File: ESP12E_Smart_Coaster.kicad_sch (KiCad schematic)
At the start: 13 parts

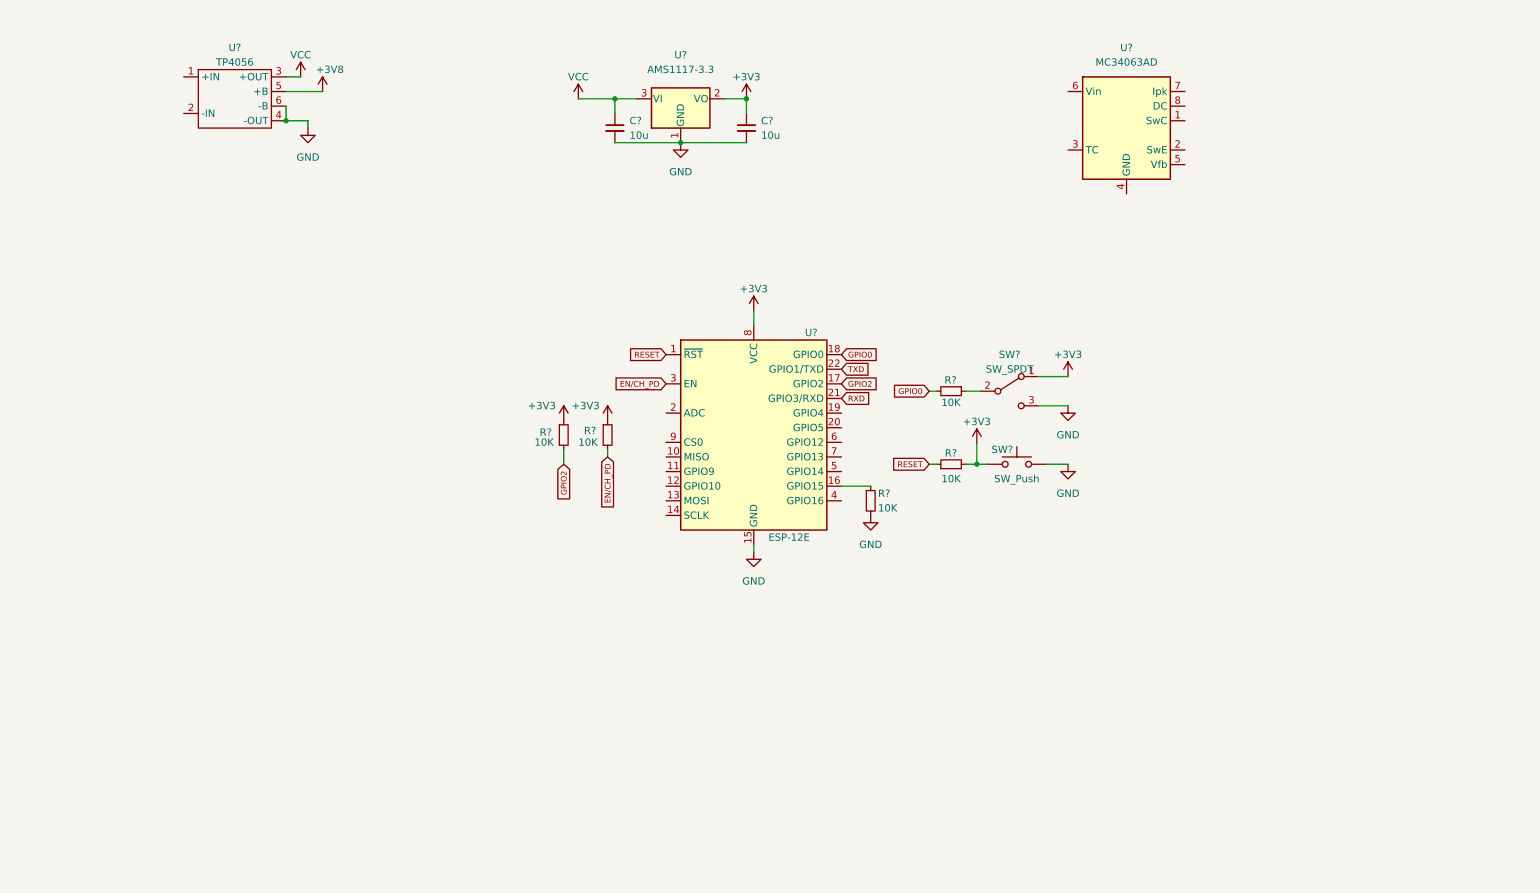
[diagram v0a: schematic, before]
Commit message: Adds WS2812B Leds & Logic Level Shifter in schematic
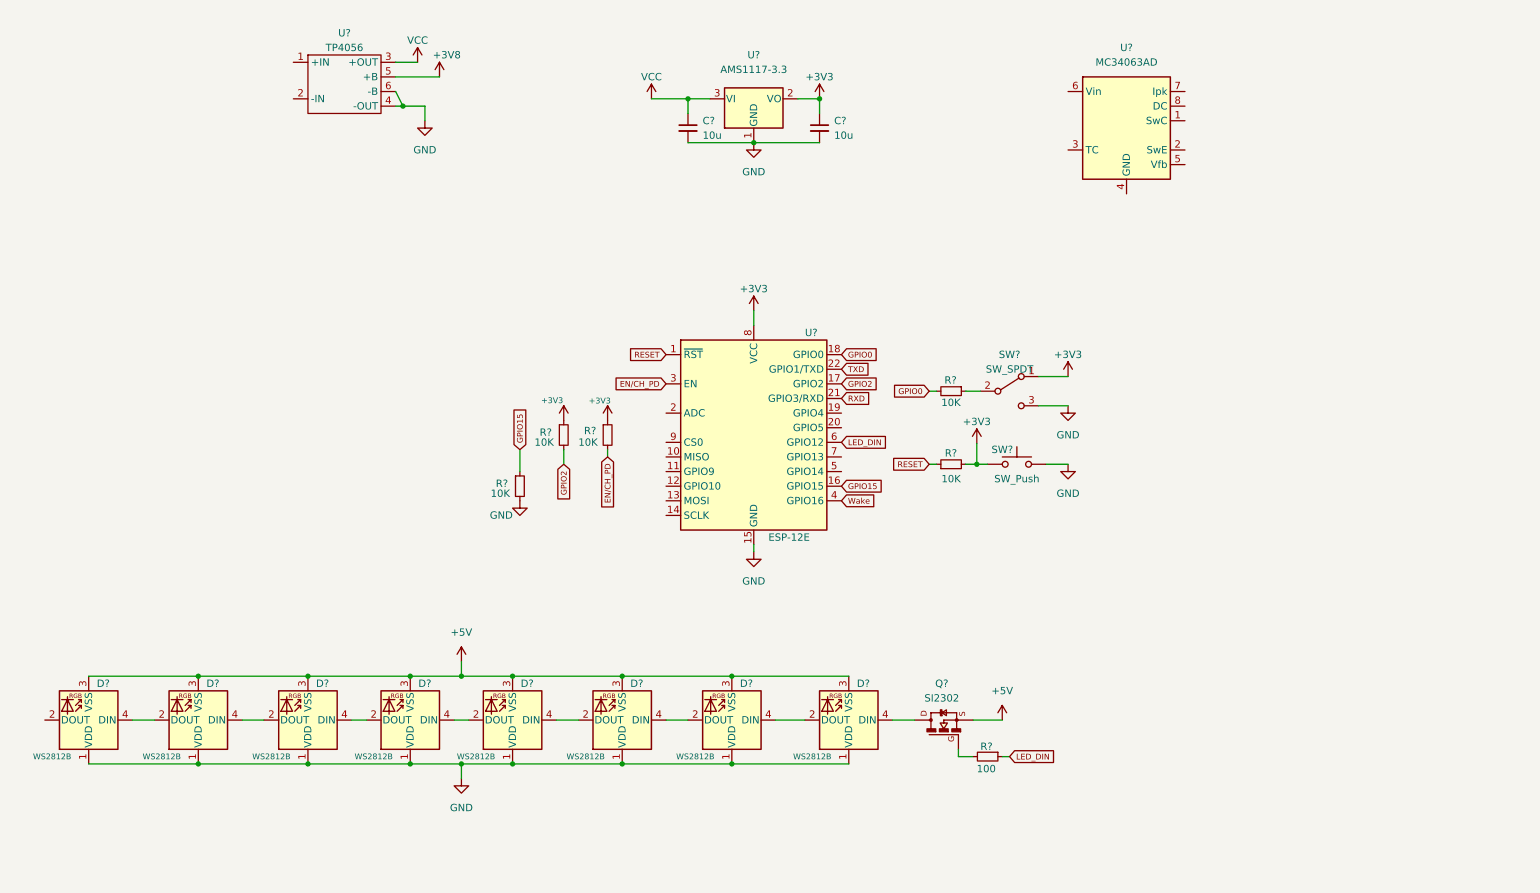
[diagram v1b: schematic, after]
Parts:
- removed R?: 10K, symbol Device:R_Small
- added D? (x8): WS2812B, LED_SMD:LED_WS2812B_PLCC4_5.0x5.0mm_P3.2mm, symbol LED:WS2812B
- added Q?: SI2302, SOT23, symbol SI2302:SI2302
- added R?: 10K, symbol Device:R_Small
- added R?: 100, symbol Device:R_Small
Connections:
- net GND: now also D?.1 (VDD), D?.1 (VDD), D?.1 (VDD), D?.1 (VDD), D?.1 (VDD), D?.1 (VDD), D?.1 (VDD), D?.1 (VDD), R?.2
- net GPIO15: now reaches U?.16 (GPIO15)
- net GPIO15: now also R?.1
- net Wake: now reaches U?.4 (GPIO16)
- net LED_DIN: now reaches U?.6 (GPIO12)
- net LED_DIN: now also R?.1
- new net: D?.2 (DOUT), D?.4 (DIN) (x7)
- new net: D?.4 (DIN), Q?.3
- new net: Q?.1, R?.2
- new net +5V: D?.3 (VSS), D?.3 (VSS), D?.3 (VSS), D?.3 (VSS), D?.3 (VSS), D?.3 (VSS), D?.3 (VSS), D?.3 (VSS), Q?.2
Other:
- moved on the sheet: C?, U?

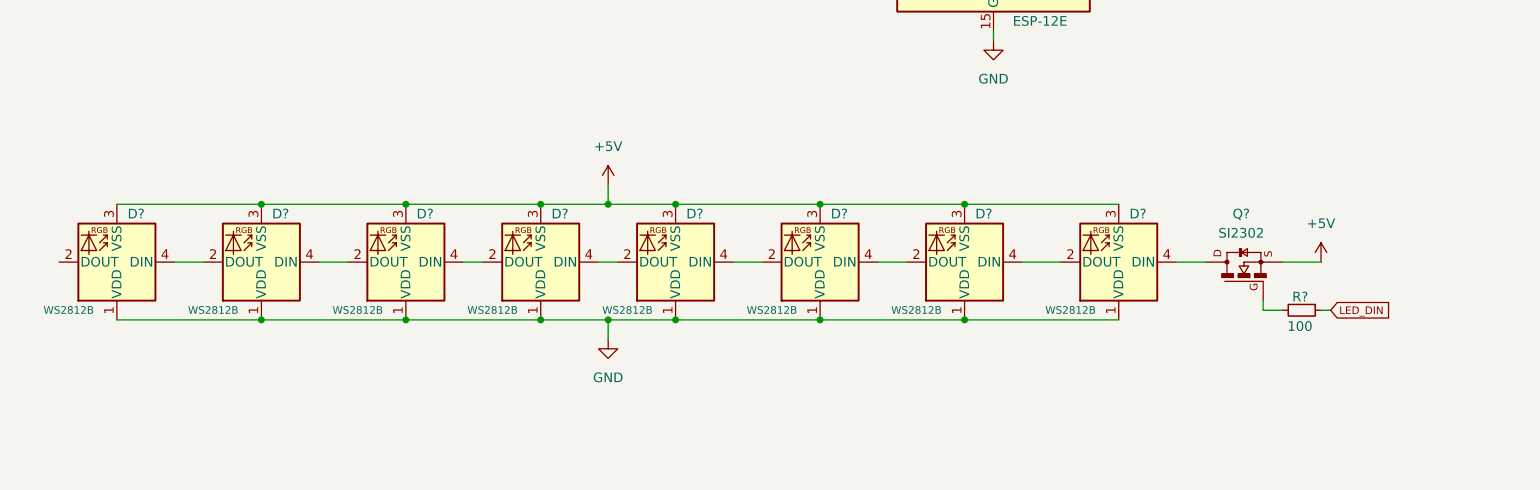
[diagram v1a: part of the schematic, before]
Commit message: Adds 0.1uF cap to WS2812B LEDs
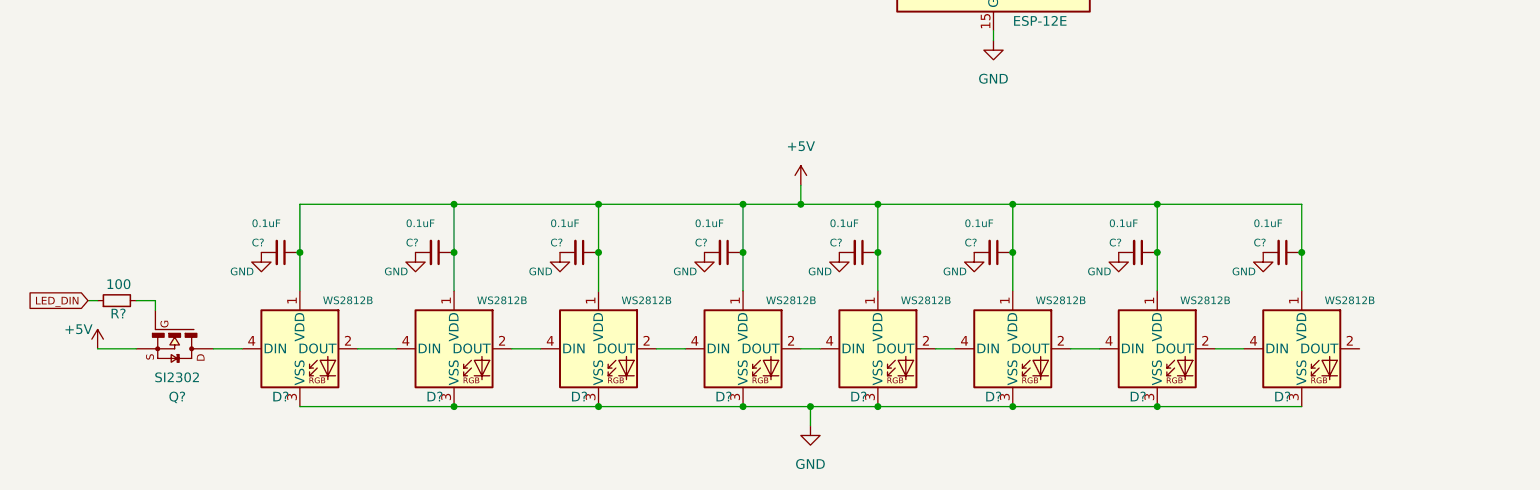
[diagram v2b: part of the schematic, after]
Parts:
- added C? (x8): 0.1uF, symbol Device:C_Small
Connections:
- net +5V: now also D?.1 (VDD), D?.1 (VDD), D?.1 (VDD), D?.1 (VDD), D?.1 (VDD), D?.1 (VDD), D?.1 (VDD), D?.1 (VDD), C?.1, C?.1, C?.1, C?.1, C?.1, C?.1, C?.1, C?.1; no longer D?.3 (VSS), D?.3 (VSS), D?.3 (VSS), D?.3 (VSS), D?.3 (VSS), D?.3 (VSS), D?.3 (VSS), D?.3 (VSS)
- net GND: now also D?.3 (VSS), D?.3 (VSS), D?.3 (VSS), D?.3 (VSS), D?.3 (VSS), D?.3 (VSS), D?.3 (VSS), D?.3 (VSS), C?.2, C?.2, C?.2, C?.2, C?.2, C?.2, C?.2, C?.2; no longer D?.1 (VDD), D?.1 (VDD), D?.1 (VDD), D?.1 (VDD), D?.1 (VDD), D?.1 (VDD), D?.1 (VDD), D?.1 (VDD)
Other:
- moved on the sheet: D?, Q?, R?

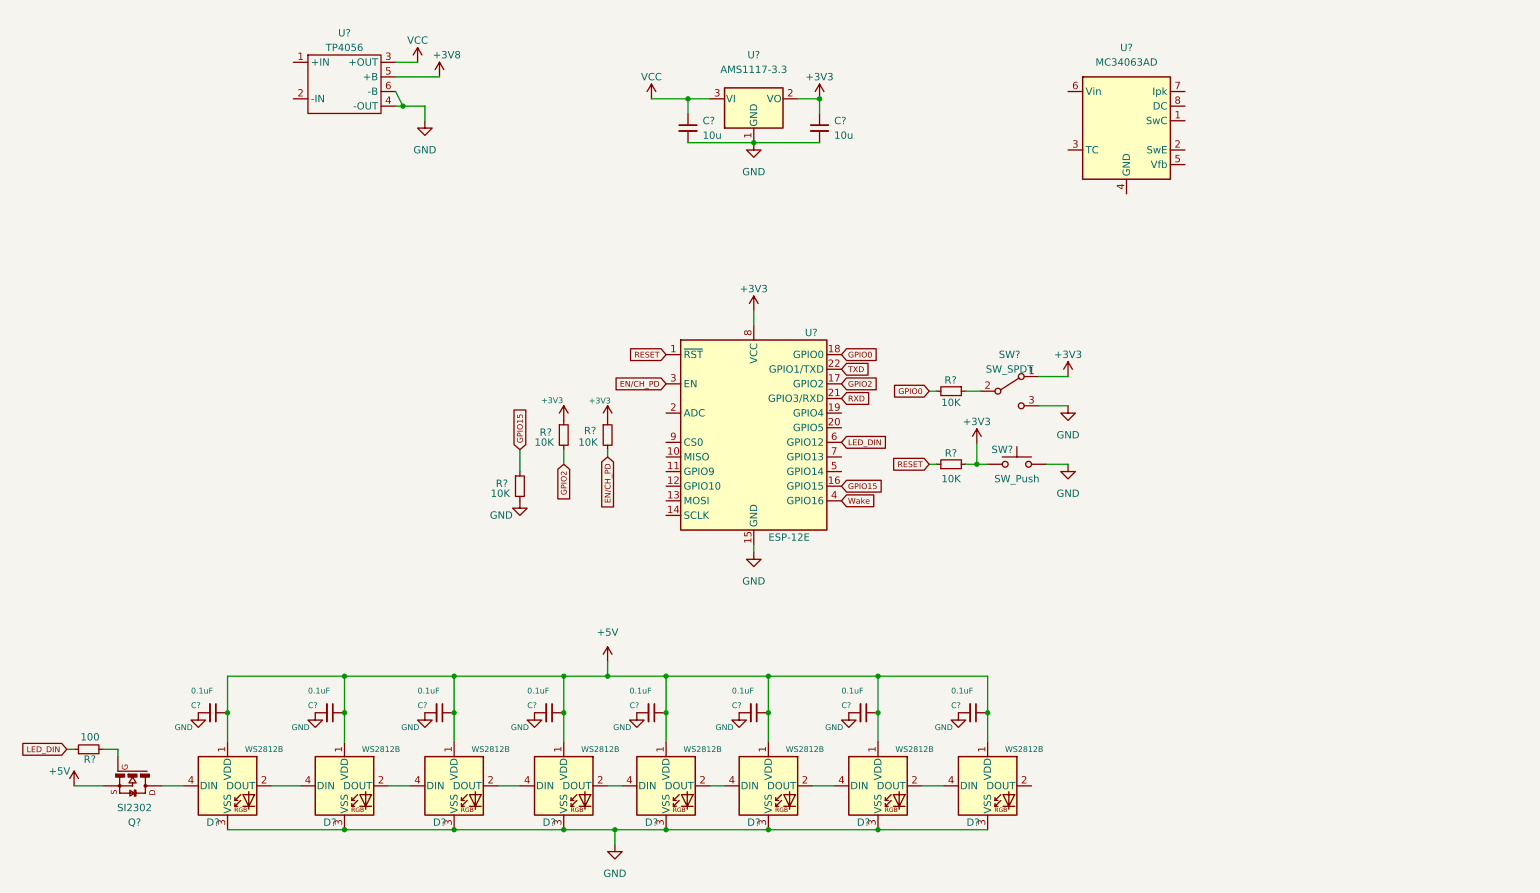
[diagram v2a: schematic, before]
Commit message: Adds library for power bank module and symbol in schematic
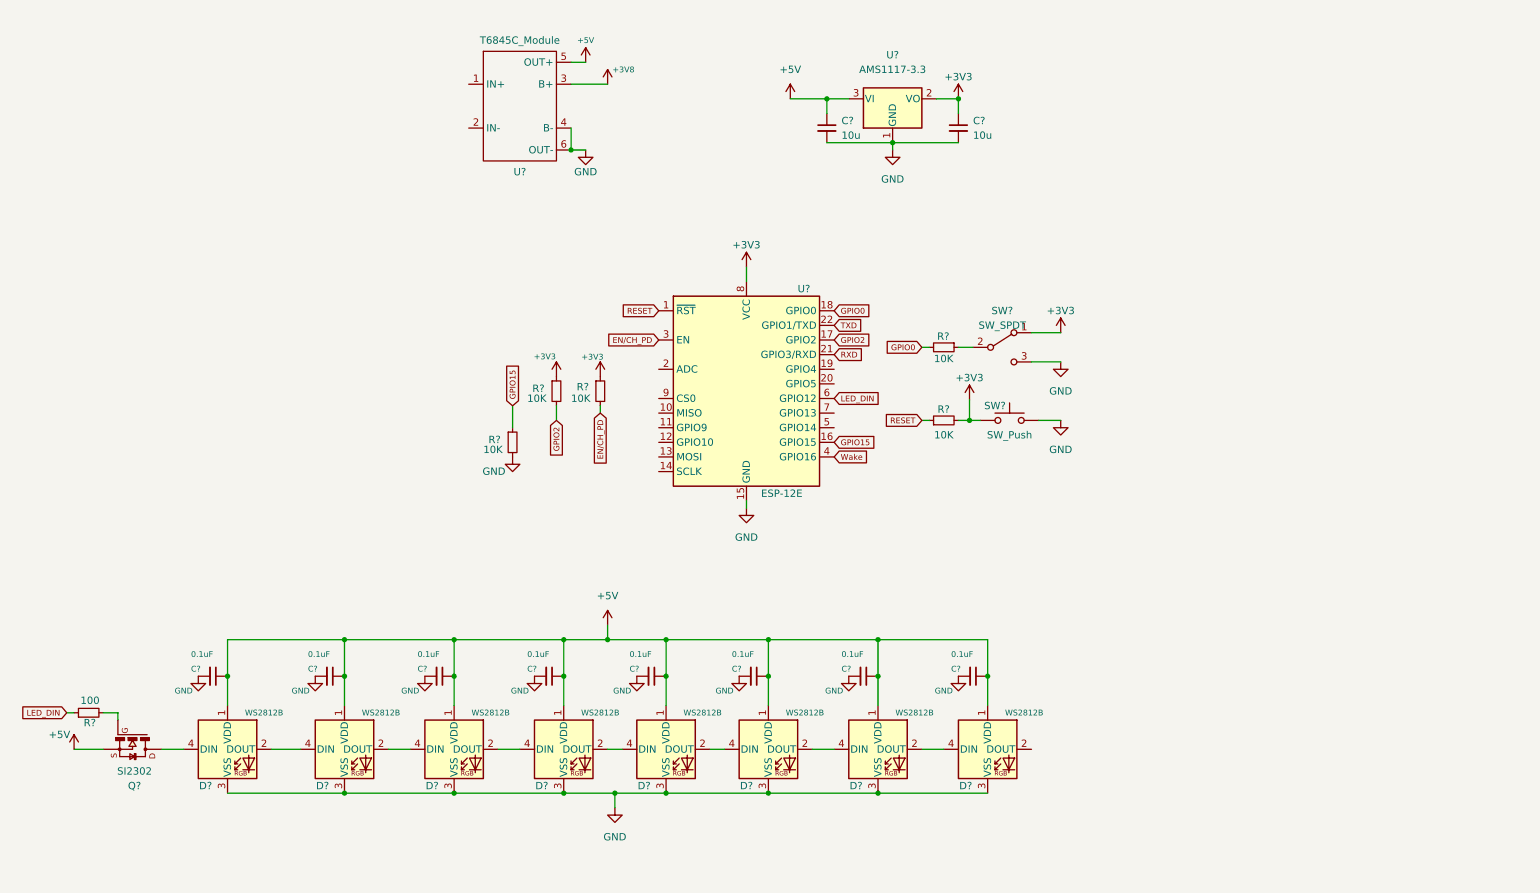
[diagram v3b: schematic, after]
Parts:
- removed U?: TP4056, symbol TP4056_Module:TP4056
- removed U?: MC34063AD, Package_SO:SOIC-8_3.9x4.9mm_P1.27mm, symbol Regulator_Switching:MC34063AD
- added U?: T6845C_Module, symbol Power_Bank_Module:T6845C_Module
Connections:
- net VCC is gone; now on net +5V: C?.1, U?.3 (VI)
- net +3V8: now also U?.3 (B+)
- net +5V: now also U?.5 (OUT+)
- net GND: now also U?.4 (B-), U?.6 (OUT-)
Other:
- moved on the sheet: C?, D?, Q?, R?, SW?, U?

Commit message: Adds footprints for components
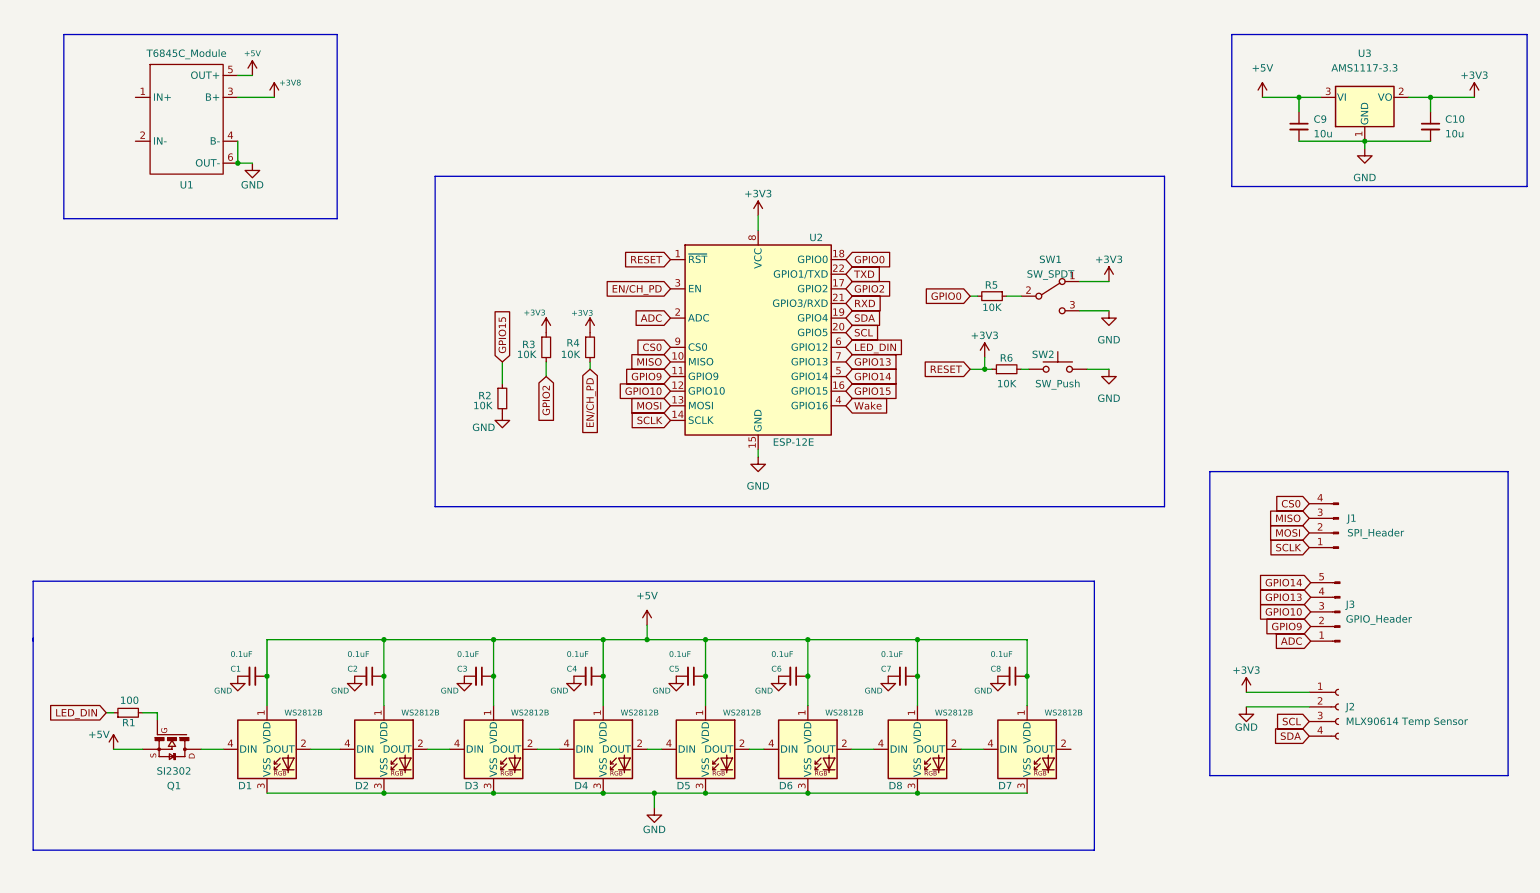
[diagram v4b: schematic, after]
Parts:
- added J1: SPI_Header, Connector_PinHeader_2.54mm:PinHeader_1x04_P2.54mm_Vertical, symbol Connector:Conn_01x04_Male
- added J2: MLX90614 Temp Sensor, Connector_PinHeader_2.54mm:PinHeader_1x04_P2.54mm_Vertical, symbol Connector:Conn_01x04_Female
- added J3: GPIO_Header, Connector_PinHeader_2.54mm:PinHeader_1x05_P2.54mm_Vertical, symbol Connector:Conn_01x05_Male
- C1, C10, C2, C3, C4, C5, C6, C7, C8, C9: renamed from C?; footprint (none) -> Capacitor_SMD:C_1206_3216Metric_Pad1.33x1.80mm_HandSolder
- Q1: renamed from Q?; footprint SOT23 -> Package_TO_SOT_SMD:SOT-23
- R1, R2, R3, R4, R5, R6: renamed from R?; footprint (none) -> Resistor_SMD:R_1206_3216Metric_Pad1.30x1.75mm_HandSolder
- gave numbers to parts that had none: 13
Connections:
- net RESET is gone; now on net +3V3: R6.1, U2.1 (~{RST})
- net +3V3: now also J2.1 (Pin_1); no longer R6.2, SW2.1
- net GND: now also J2.2 (Pin_2)
- net MISO: now reaches U2.10 (MISO)
- net MISO: now also J1.3 (Pin_3)
- net GPIO9: now reaches U2.11 (GPIO9)
- net GPIO9: now also J3.2 (Pin_2)
- net GPIO10: now reaches U2.12 (GPIO10)
- net GPIO10: now also J3.3 (Pin_3)
- net MOSI: now reaches U2.13 (MOSI)
- net MOSI: now also J1.2 (Pin_2)
- net SCLK: now reaches U2.14 (SCLK)
- net SCLK: now also J1.1 (Pin_1)
- net SDA: now reaches U2.19 (GPIO4)
- net SDA: now also J2.4 (Pin_4)
- net ADC: now reaches U2.2 (ADC)
- net ADC: now also J3.1 (Pin_1)
- net SCL: now reaches U2.20 (GPIO5)
- net SCL: now also J2.3 (Pin_3)
- net GPIO14: now reaches U2.5 (GPIO14)
- net GPIO14: now also J3.5 (Pin_5)
- net GPIO13: now reaches U2.7 (GPIO13)
- net GPIO13: now also J3.4 (Pin_4)
- net CS0: now reaches U2.9 (CS0)
- net CS0: now also J1.4 (Pin_4)
- new net: R6.2, SW2.1
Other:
- moved on the sheet: C1, C10, C2, C3, C4, C5, C6, C7, C8, C9, D1, D2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

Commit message: added footprint for spdt and push switches
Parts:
- SW1: footprint (none) -> Button_Switch_THT:SW_CuK_OS102011MA1QN1_SPDT_Angled
- SW2, U1: footprint (none) -> Button_Switch_SMD:SW_Push_SPST_NO_Alps_SKRK
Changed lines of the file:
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@@
     (property "Reference" "SW1" (id 0) (at 196.342 60.96 0))
     (property "Value" "SW_SPDT" (id 1) (at 196.342 63.5 0))
-    (property "Footprint" "" (id 2) (at 196.342 67.31 0)
+    (property "Footprint" "Button_Switch_THT:SW_CuK_OS102011MA1QN1_SPDT_Angled" (id 2) (at 196.342 67.31 0)
       (effects (font (size 1.27 1.27)) hide)
     )
@@
     (property "Reference" "SW2" (id 0) (at 195.072 77.47 0))
     (property "Value" "SW_Push" (id 1) (at 197.612 82.55 0))
-    (property "Footprint" "" (id 2) (at 197.612 74.93 0)
+    (property "Footprint" "Button_Switch_SMD:SW_Push_SPST_NO_Alps_SKRK" (id 2) (at 197.612 74.93 0)
       (effects (font (size 1.27 1.27)) hide)
     )
@@
     (property "Reference" "U1" (id 0) (at 46.228 48.006 0))
     (property "Value" "T6845C_Module" (id 1) (at 46.228 25.146 0))
-    (property "Footprint" "" (id 2) (at 47.498 36.576 0)
+    (property "Footprint" "Button_Switch_SMD:SW_Push_SPST_NO_Alps_SKRK" (id 2) (at 47.498 36.576 0)
       (effects (font (size 1.27 1.27)) hide)
     )
@@
     )
     (path "/465fa1d7-438a-4179-8f7b-17a5edbc6ac2"
-      (reference "SW1") (unit 1) (value "SW_SPDT") (footprint "")
+      (reference "SW1") (unit 1) (value "SW_SPDT") (footprint "Button_Switch_THT:SW_CuK_OS102011MA1QN1_SPDT_Angled")
     )
     (path "/689e8e86-37e1-4740-9e66-5c53a4404734"
-      (reference "SW2") (unit 1) (value "SW_Push") (footprint "")
+      (reference "SW2") (unit 1) (value "SW_Push") (footprint "Button_Switch_SMD:SW_Push_SPST_NO_Alps_SKRK")
     )
     (path "/cb6274d7-f31a-45f6-9679-0c3033833f41"
-      (reference "U1") (unit 1) (value "T6845C_Module") (footprint "")
+      (reference "U1") (unit 1) (value "T6845C_Module") (footprint "Button_Switch_SMD:SW_Push_SPST_NO_Alps_SKRK")
     )
     (path "/eacb41d9-aa3d-4548-904e-3f363a3c1aac"
